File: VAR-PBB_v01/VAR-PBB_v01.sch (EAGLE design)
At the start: 32 parts, among them J1 ANDERSON_POWER_POLE, J11 CON1X2_SHROUDED, J2 ANDERSON_POWER_POLE, J3 CON1X2_SHROUDED, J4 CON1X2_SHROUDED, J5 CON1X2_SHROUDED, J6 CON1X2_SHROUDED, J7 CON1X2_SHROUDED, J8 CON1X2_SHROUDED, U1 OKI-78SR, U2 XL6009, U3 XL6009, U4 XL6009, U5 LP2985AIM5-1.5, U6 TPS259271DRCR

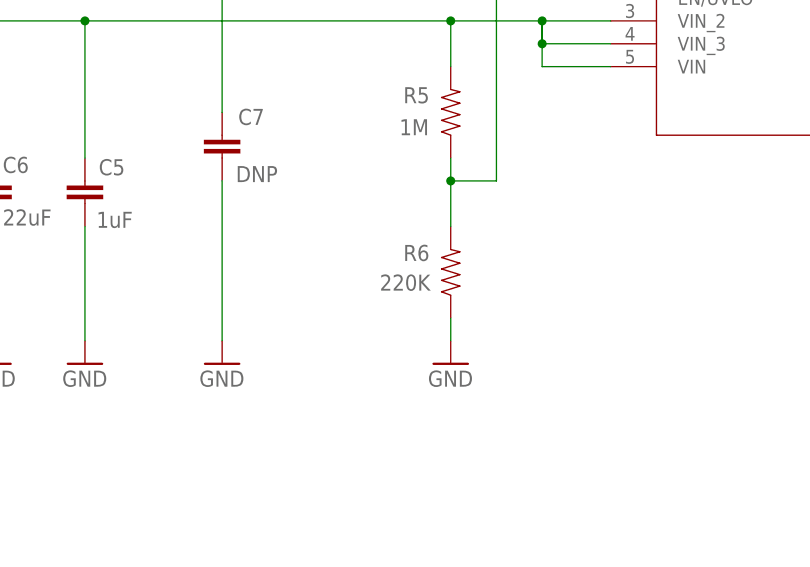
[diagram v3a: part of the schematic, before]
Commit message: Latest version of VAR-PBB, as built. Updated under voltage cutout resistor to get UVLO to around 8.1 V.
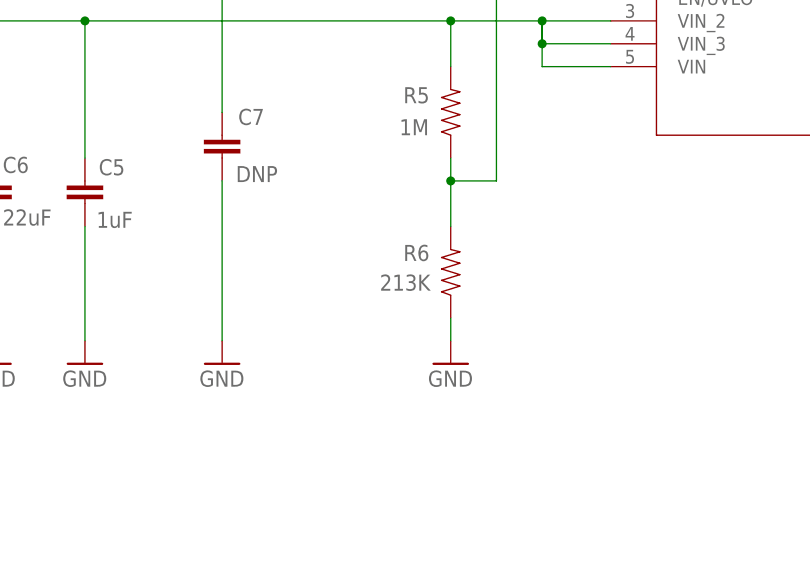
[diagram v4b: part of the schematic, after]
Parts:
- R6: value 220K -> 213K
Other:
- note added: "E-Fuse Provides: - Undervoltage Lock Out (UVLO) (7.97V default) - Over Current Protection (Set to 2.1A max)"
- note removed: "E-Fuse Provides: - Undervoltage Lock Out (UVLO) (8V default) - Over Current Protection (Set to 2.1A max)"
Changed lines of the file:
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@@
 <grid distance="0.1" unitdist="inch" unit="inch" style="lines" multiple="1" display="no" altdistance="0.01" altunitdist="inch" altunit="inch"/>
 <layers>
-<layer number="1" name="Top" color="4" fill="1" visible="yes" active="no"/>
-<layer number="2" name="Route2" color="1" fill="3" visible="yes" active="no"/>
-<layer number="3" name="Route3" color="4" fill="3" visible="yes" active="no"/>
-<layer number="4" name="Route4" color="1" fill="4" visible="yes" active="no"/>
-<layer number="5" name="Route5" color="4" fill="4" visible="yes" active="no"/>
-<layer number="6" name="Route6" color="1" fill="8" visible="yes" active="no"/>
-<layer number="7" name="Route7" color="4" fill="8" visible="yes" active="no"/>
-<layer number="8" name="Route8" color="1" fill="2" visible="yes" active="no"/>
-<layer number="9" name="Route9" color="4" fill="2" visible="yes" active="no"/>
-<layer number="10" name="Route10" color="1" fill="7" visible="yes" active="no"/>
-<layer number="11" name="Route11" color="4" fill="7" visible="yes" active="no"/>
-<layer number="12" name="Route12" color="1" fill="5" visible="yes" active="no"/>
-<layer number="13" name="Route13" color="4" fill="5" visible="yes" active="no"/>
-<layer number="14" name="Route14" color="1" fill="6" visible="yes" active="no"/>
-<layer number="15" name="Route15" color="4" fill="6" visible="yes" active="no"/>
-<layer number="16" name="Bottom" color="1" fill="1" visible="yes" active="no"/>
-<layer number="17" name="Pads" color="2" fill="1" visible="yes" active="no"/>
-<layer number="18" name="Vias" color="2" fill="1" visible="yes" active="no"/>
-<layer number="19" name="Unrouted" color="6" fill="1" visible="yes" active="no"/>
-<layer number="20" name="Dimension" color="15" fill="1" visible="yes" active="no"/>
-<layer number="21" name="tPlace" color="7" fill="1" visible="yes" active="no"/>
-<layer number="22" name="bPlace" color="7" fill="1" visible="yes" active="no"/>
-<layer number="23" name="tOrigins" color="15" fill="1" visible="yes" active="no"/>
-<layer number="24" name="bOrigins" color="15" fill="1" visible="yes" active="no"/>
-<layer number="25" name="tNames" color="7" fill="1" visible="yes" active="no"/>
-<layer number="26" name="bNames" color="7" fill="1" visible="yes" active="no"/>
-<layer number="27" name="tValues" color="7" fill="1" visible="yes" active="no"/>
-<layer number="28" name="bValues" color="7" fill="1" visible="yes" active="no"/>
+<layer number="1" name="Top" color="4" fill="1" visible="no" active="no"/>
+<layer number="2" name="Route2" color="1" fill="3" visible="no" active="no"/>
+<layer number="3" name="Route3" color="4" fill="3" visible="no" active="no"/>
+<layer number="4" name="Route4" color="1" fill="4" visible="no" active="no"/>
+<layer number="5" name="Route5" color="4" fill="4" visible="no" active="no"/>
+<layer number="6" name="Route6" color="1" fill="8" visible="no" active="no"/>
+<layer number="7" name="Route7" color="4" fill="8" visible="no" active="no"/>
+<layer number="8" name="Route8" color="1" fill="2" visible="no" active="no"/>
+<layer number="9" name="Route9" color="4" fill="2" visible="no" active="no"/>
+<layer number="10" name="Route10" color="1" fill="7" visible="no" active="no"/>
+<layer number="11" name="Route11" color="4" fill="7" visible="no" active="no"/>
+<layer number="12" name="Route12" color="1" fill="5" visible="no" active="no"/>
+<layer number="13" name="Route13" color="4" fill="5" visible="no" active="no"/>
+<layer number="14" name="Route14" color="1" fill="6" visible="no" active="no"/>
+<layer number="15" name="Route15" color="4" fill="6" visible="no" active="no"/>
+<layer number="16" name="Bottom" color="1" fill="1" visible="no" active="no"/>
+<layer number="17" name="Pads" color="2" fill="1" visible="no" active="no"/>
+<layer number="18" name="Vias" color="2" fill="1" visible="no" active="no"/>
+<layer number="19" name="Unrouted" color="6" fill="1" visible="no" active="no"/>
+<layer number="20" name="Dimension" color="15" fill="1" visible="no" active="no"/>
+<layer number="21" name="tPlace" color="7" fill="1" visible="no" active="no"/>
+<layer number="22" name="bPlace" color="7" fill="1" visible="no" active="no"/>
+<layer number="23" name="tOrigins" color="15" fill="1" visible="no" active="no"/>
+<layer number="24" name="bOrigins" color="15" fill="1" visible="no" active="no"/>
+<layer number="25" name="tNames" color="7" fill="1" visible="no" active="no"/>
+<layer number="26" name="bNames" color="7" fill="1" visible="no" active="no"/>
+<layer number="27" name="tValues" color="7" fill="1" visible="no" active="no"/>
+<layer number="28" name="bValues" color="7" fill="1" visible="no" active="no"/>
 <layer number="29" name="tStop" color="7" fill="3" visible="no" active="no"/>
 <layer number="30" name="bStop" color="7" fill="6" visible="no" active="no"/>
@@
 <layer number="35" name="tGlue" color="7" fill="4" visible="no" active="no"/>
 <layer number="36" name="bGlue" color="7" fill="5" visible="no" active="no"/>
-<layer number="37" name="tTest" color="7" fill="1" visible="yes" active="no"/>
-<layer number="38" name="bTest" color="7" fill="1" visible="yes" active="no"/>
+<layer number="37" name="tTest" color="7" fill="1" visible="no" active="no"/>
+<layer number="38" name="bTest" color="7" fill="1" visible="no" active="no"/>
 <layer number="39" name="tKeepout" color="4" fill="11" visible="no" active="no"/>
 <layer number="40" name="bKeepout" color="1" fill="11" visible="no" active="no"/>
@@
 <layer number="44" name="Drills" color="7" fill="1" visible="no" active="no"/>
 <layer number="45" name="Holes" color="7" fill="1" visible="no" active="no"/>
-<layer number="46" name="Milling" color="3" fill="1" visible="yes" active="no"/>
-<layer number="47" name="Measures" color="7" fill="1" visible="yes" active="no"/>
-<layer number="48" name="Document" color="7" fill="1" visible="yes" active="no"/>
-<layer number="49" name="Reference" color="7" fill="1" visible="yes" active="no"/>
-<layer number="50" name="dxf" color="7" fill="1" visible="yes" active="no"/>
-<layer number="51" name="tDocu" color="7" fill="1" visible="yes" active="no"/>
-<layer number="52" name="bDocu" color="7" fill="1" visible="yes" active="no"/>
-<layer number="53" name="tGND_GNDA" color="7" fill="9" visible="yes" active="no"/>
-<layer number="54" name="bGND_GNDA" color="1" fill="9" visible="yes" active="no"/>
-<layer number="56" name="wert" color="7" fill="1" visible="yes" active="no"/>
-<layer number="57" name="tCAD" color="7" fill="1" visible="yes" active="no"/>
-<layer number="59" name="tCarbon" color="7" fill="1" visible="yes" active="no"/>
-<layer number="60" name="bCarbon" color="7" fill="1" visible="yes" active="no"/>
+<layer number="46" name="Milling" color="3" fill="1" visible="no" active="no"/>
+<layer number="47" name="Measures" color="7" fill="1" visible="no" active="no"/>
+<layer number="48" name="Document" color="7" fill="1" visible="no" active="no"/>
+<layer number="49" name="Reference" color="7" fill="1" visible="no" active="no"/>
+<layer number="50" name="dxf" color="7" fill="1" visible="no" active="no"/>
+<layer number="51" name="tDocu" color="7" fill="1" visible="no" active="no"/>
+<layer number="52" name="bDocu" color="7" fill="1" visible="no" active="no"/>
+<layer number="53" name="tGND_GNDA" color="7" fill="9" visible="no" active="no"/>
+<layer number="54" name="bGND_GNDA" color="1" fill="9" visible="no" active="no"/>
+<layer number="56" name="wert" color="7" fill="1" visible="no" active="no"/>
+<layer number="57" name="tCAD" color="7" fill="1" visible="no" active="no"/>
+<layer number="59" name="tCarbon" color="7" fill="1" visible="no" active="no"/>
+<layer number="60" name="bCarbon" color="7" fill="1" visible="no" active="no"/>
 <layer number="88" name="SimResults" color="9" fill="1" visible="yes" active="yes"/>
 <layer number="89" name="SimProbes" color="9" fill="1" visible="yes" active="yes"/>
@@
 <part name="GND15" library="SparkFun" deviceset="GND" device=""/>
 <part name="R5" library="SparkFun-Resistors" library_urn="urn:adsk.eagle:library:532" deviceset="RESISTOR" device="0603" package3d_urn="urn:adsk.eagle:package:39650/1" value="1M"/>
-<part name="R6" library="SparkFun-Resistors" library_urn="urn:adsk.eagle:library:532" deviceset="RESISTOR" device="0603" package3d_urn="urn:adsk.eagle:package:39650/1" value="220K"/>
+<part name="R6" library="SparkFun-Resistors" library_urn="urn:adsk.eagle:library:532" deviceset="RESISTOR" device="0603" package3d_urn="urn:adsk.eagle:package:39650/1" value="213K"/>
 <part name="GND16" library="SparkFun" deviceset="GND" device=""/>
 <part name="GND17" library="SparkFun" deviceset="GND" device=""/>
@@
 Provides:
 - Undervoltage Lock Out (UVLO)
-  (8V default)
+  (7.97V default)
 - Over Current Protection
   (Set to 2.1A max)</text>
